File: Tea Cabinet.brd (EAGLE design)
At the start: 51.7 x 26.7 mm, 14 parts, among them IC1 74LS00N, IC2 74LS74N, IC3 5V, IC4 12V, Q1 2N3904

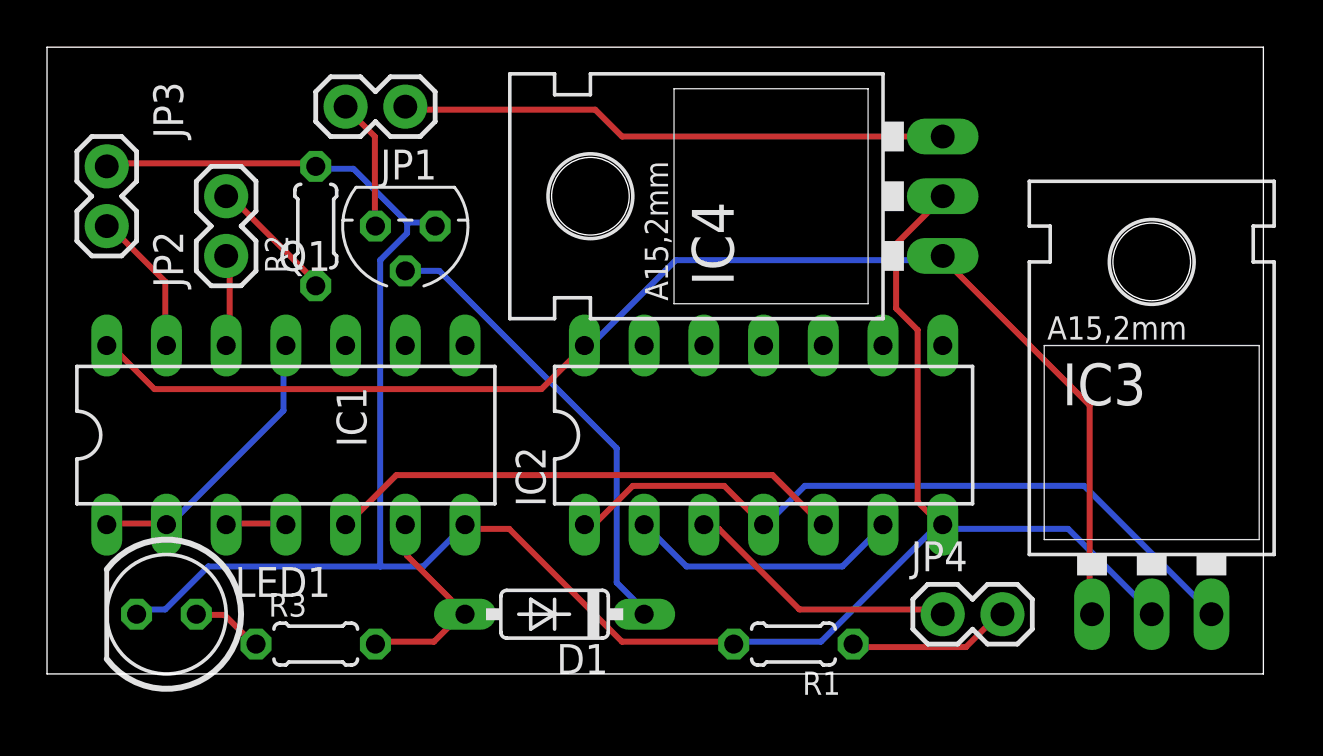
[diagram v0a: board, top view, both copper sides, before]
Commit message: Made the board more compact
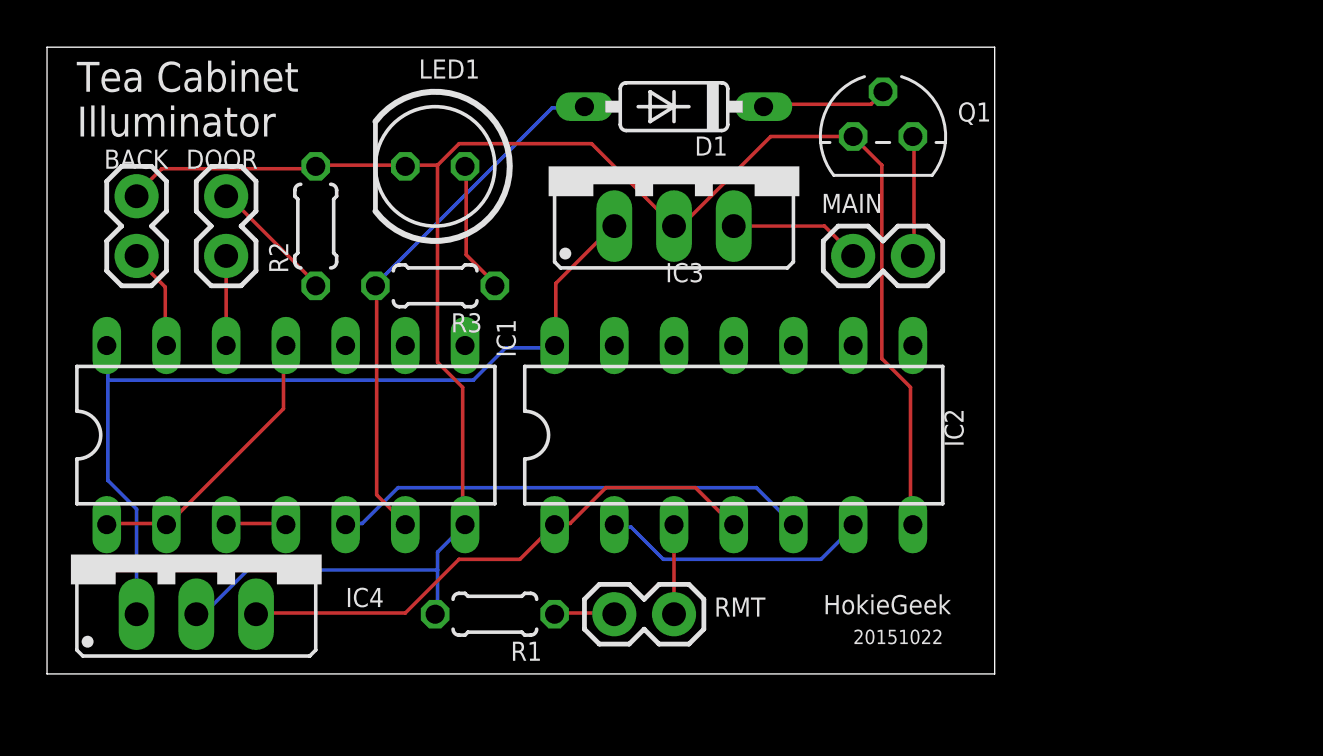
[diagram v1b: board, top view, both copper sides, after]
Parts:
- removed JP1, JP3, JP4: (no value), SparkFun:1X02
- added BACK, MAIN, RMT: (no value), SparkFun:1X02
- IC3: value 5V -> 12V; device v-reg:78XXL -> v-reg:78XXS
- IC4: value 12V -> 5V; device v-reg:78XXL -> v-reg:78XXS
- moved IC4 31.8 mm to (6.35, 5.08), turned to 0 degrees
- moved IC3 25.4 mm to (26.7, 21.6)
- moved LED1 22.2 mm to (16.5, 21.6)
- moved D1 22.2 mm to (26.7, 24.1)
- moved Q1 20.7 mm to (35.6, 22.9), turned to 0 degrees
- moved R3 16.1 mm to (16.5, 16.5), turned to 180 degrees
- moved R1 12.8 mm to (19.1, 2.54)
- moved IC2 1.27 mm to (29.2, 10.2)
- renumbered JP2 to DOOR
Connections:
- net 12V: now also IC3.OUT, MAIN.1; no longer IC4.OUT, JP1.1
- net 5V: now also IC4.OUT; no longer IC3.OUT
- net BACK: now also BACK.1; no longer JP3.1
- net GND: now also BACK.2; no longer JP3.2
- net N$2: now also MAIN.2; no longer JP1.2
- net N$4: now also RMT.2; no longer JP4.2
- net RMT: now also RMT.1; no longer JP4.1
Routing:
- net VCC: track 56.6 -> 37.7 mm
- net 12V: track 23.4 -> 5.64 mm
- net N$3: track 19.7 -> 5.41 mm
- net N$6: track 9.15 -> 22.8 mm
- net GND: track 96.8 -> 83.4 mm
- net RMT: track 11.8 -> 3.81 mm
- net 5V: track 31.0 -> 23.2 mm
- net N$4: track 7.05 -> 2.58 mm
- net N$1: track 3.04 -> 5.60 mm
- net BACK: track 6.17 -> 4.34 mm
- net N$9: track 22.0 -> 20.3 mm
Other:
- board size 51.7 x 26.7 mm -> 40.3 x 26.7 mm
- board text added: "20151022"
- board text added: "HokieGeek"
- board text added: "Tea Cabinet Illuminator"
